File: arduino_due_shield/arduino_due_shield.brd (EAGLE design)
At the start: 101.6 x 53.3 mm, 27 parts, among them J12 ARDUINO_MEGA_R3FULL, J13 POLOLU-2595, J14 POLOLU-2807, J15 POLOLU-2595

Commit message: Finish schematic and PCB design
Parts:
- removed R4: 3.3k, resistor:0204/7
- removed R5: 2.2k, resistor:0204/7
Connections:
- net RX1 renamed RC_RX1
- net RX2 renamed RC_RX2
- net RX3 renamed RC_RX3
- removed net RELAYHV: JP11.2, R4.2
- new net N$2: J14.FAILMODE1, J14.FAILMODE2
- new net RELAYOUT_HV: J13.H4, JP11.2
- net GND: no longer R5.1
- net RELAYOUT: now also J13.L4; no longer R4.1, R5.2
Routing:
- net RELAYOUT_HV: track 0.00 -> 76.5 mm, vias 0 -> 2
- net RELAYHV: track 73.2 -> 0.00 mm, vias 1 -> 0
- net RELAYOUT: track 15.0 -> 32.1 mm
- net N$2: track 0.00 -> 5.61 mm
- net GND: track 0.00 -> 2.54 mm
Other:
- board text added: "AutoRally Arduino Due Shield, rev 1, 2019"
- board text added: "Board #"
- board text added: "Brakes"
- board text added: "Castle Link"
- board text added: "ESC"
- board text added: "Fans"
- board text added: "HV LV"
- board text added: "Receiver"
- board text added: "Relay"
- board text added: "Steering"
- board text added: "Wheel Sensors"

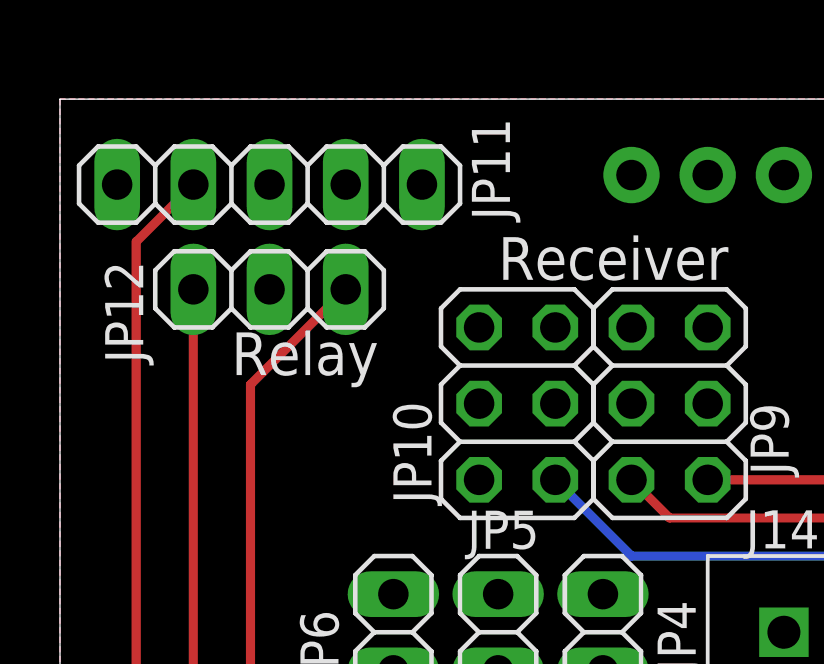
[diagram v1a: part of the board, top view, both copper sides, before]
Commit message: Add missing RC_RX4 net
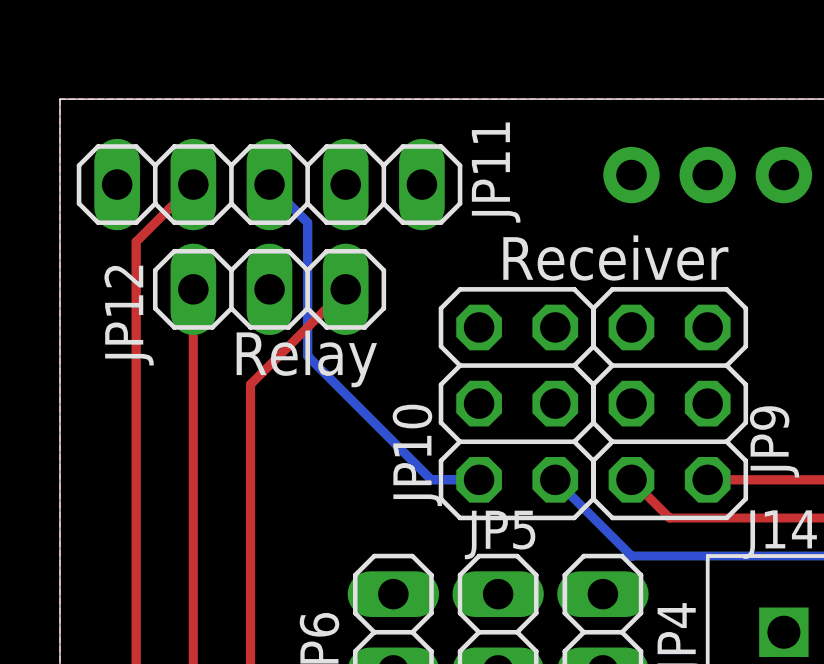
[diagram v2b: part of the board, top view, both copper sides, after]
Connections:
- removed net RX4: JP11.3
- new net RC_RX4: JP10.2, JP11.3
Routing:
- net RC_RX4: track 0.00 -> 13.7 mm
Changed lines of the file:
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@@
 <wire x1="6.35" y1="43.815" x2="6.35" y2="15.24" width="0.3048" layer="1"/>
 </signal>
-<signal name="RX4">
+<signal name="RC_RX4">
 <contactref element="JP11" pad="3"/>
+<contactref element="JP10" pad="2"/>
+<wire x1="6.985" y1="50.4825" x2="8.255" y2="49.2125" width="0.3048" layer="16"/>
+<wire x1="8.255" y1="44.7675" x2="8.255" y2="49.2125" width="0.3048" layer="16"/>
+<wire x1="13.97" y1="40.64" x2="12.3825" y2="40.64" width="0.3048" layer="16"/>
+<wire x1="12.3825" y1="40.64" x2="8.255" y2="44.7675" width="0.3048" layer="16"/>
 </signal>
 <signal name="RELAYOUT">
